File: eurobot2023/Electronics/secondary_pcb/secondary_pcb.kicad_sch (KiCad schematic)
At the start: 34 parts, among them IC1 CD74HCT125M96, IC2 SN74LVC126ADR, J1 PI40HAT, J10 Conn_01x02_Male, J11 MagneticEncoder, J12 Conn_01x07_Male, J13 MagneticEncoder, J14 Conn_01x03_Male, J15 Conn_01x02_Male, J2 Conn_01x02_Male, J3 Conn_01x02_Male, J4 Conn_01x02_Male, J5 Conn_01x02_Male, J6 Conn_01x02_Male, J7 Conn_01x02_Male, J9 22-03-5035, P1 R-78Bxx-2.0, P2 Amazon 5A stepdown, U1 MCP2515-xSO, U2 TJA1049T, U3 PCA9306D, U4 Pololu_MAX14870, U5 PCA9685PW

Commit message: Modify secondary pcb
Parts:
- removed C3: Conn_03x08, MiAM:Pin_Header_Straight_3x08_Pitch2.54mm, symbol MiAM:Conn_03x08
- removed J14: Conn_01x03_Male, Connector_PinHeader_2.54mm:PinHeader_1x03_P2.54mm_Vertical, symbol Connector:Conn_01x03_Male
- removed U3: PCA9306D, Package_SO:SO-8_3.9x4.9mm_P1.27mm, symbol Interface:PCA9306D
- removed U5: PCA9685PW, Package_SO:TSSOP-28_4.4x9.7mm_P0.65mm, symbol Driver_LED:PCA9685PW
- added I2C2, I2C3: Conn_01x05_Male, Connector_PinHeader_2.54mm:PinHeader_1x05_P2.54mm_Vertical, symbol Connector:Conn_01x05_Male
- added Mot V Select: Conn_01x03_Male, Connector_PinHeader_2.54mm:PinHeader_1x03_P2.54mm_Vertical, symbol Connector:Conn_01x03_Male
- Enc 1: renamed from J11
- Enc 2: renamed from J13
- IC1, IC2: footprint SOIC127P600X175-14N -> MiAM:SOIC127P600X175-14N
- Servo: renamed from J9; footprint SHDR3W60P0X250_1X3_990X490X590P -> MiAM:SHDR3W60P0X250_1X3_990X490X590P
- renumbered J7 to CAN1, J15 to CAN2, C4 to GPIO, J12 to I2C1, J10 to Mot
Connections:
- net +24V: now also Mot V Select.3 (Pin_3)
- net +3.3V: now also I2C2.1 (Pin_1), I2C3.1 (Pin_1)
- net +7.5V: now also Mot V Select.1 (Pin_1); no longer U4.9 (Vin)
- net GND: now also I2C2.2 (Pin_2), I2C3.2 (Pin_2)
- net I2C SCL: now also I2C2.3 (Pin_3), I2C3.3 (Pin_3)
- net I2C SDA: now also I2C2.4 (Pin_4), I2C3.4 (Pin_4)
- net GPIO 13: now reaches J1.33 (BCM13)
- net GPIO 13: now also I2C2.5 (Pin_5)
- net GPIO 19: now reaches J1.35 (BCM19)
- net GPIO 19: now also I2C3.5 (Pin_5)
- new net: Mot V Select.2 (Pin_2), U4.9 (Vin)
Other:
- note added: "DC motor"
- note added: "Encoders"
- note added: "Raspberry Pi"
- note removed: "Pump & other DC motor"
- note removed: "RC servos"
- note removed: "Servo driver"
- note removed: "[TODO] - Transistor for power switch"
- company: (none) -> MiAM Robotics Inc.
- title: (none) -> Secondary Robot PCB
- moved on the sheet: C1, C2, CAN1, CAN2, D2, D3, Enc 1, Enc 2, GPIO, HC49, I2C1, IC1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

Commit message: Begin routing
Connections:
- net UART_RX_5 is gone; now on net UART_HD: IC2.5 (2A)
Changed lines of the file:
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@@
     (effects (font (size 1.27 1.27)) (justify left bottom))
   )
-  (label "UART_RX_5" (at 115.57 95.25 180)
+  (label "UART_HD" (at 115.57 95.25 180)
     (effects (font (size 1.27 1.27)) (justify right bottom))
   )

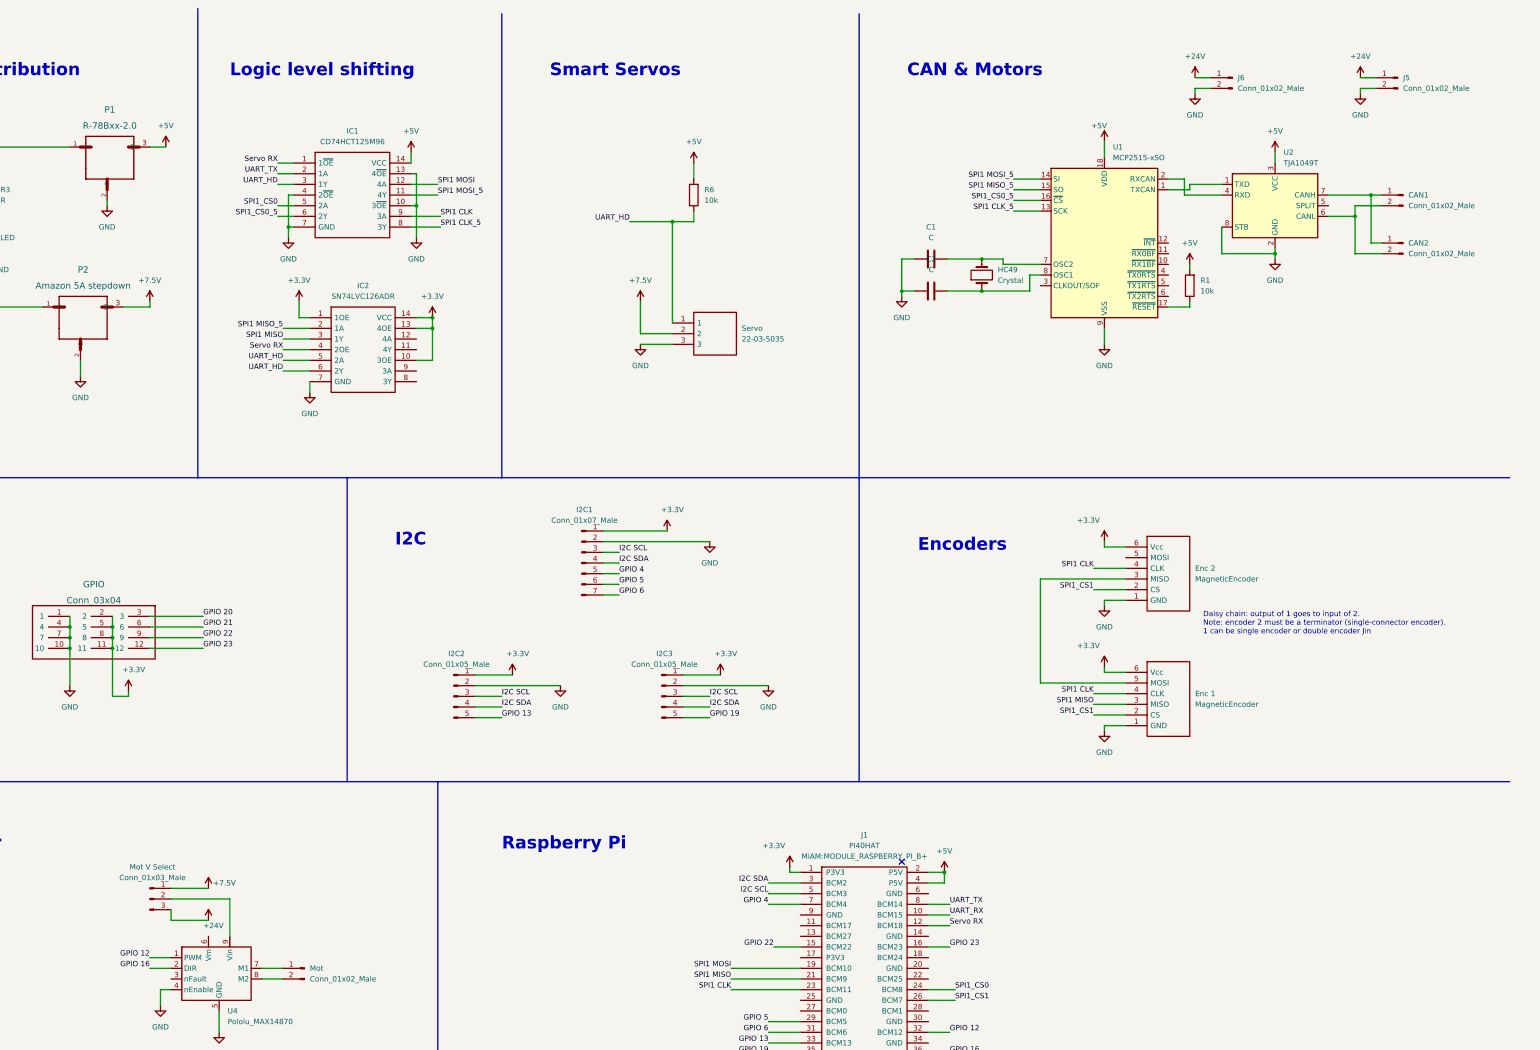
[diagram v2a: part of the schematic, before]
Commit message: Electronics: correct PCB schematic and component references.
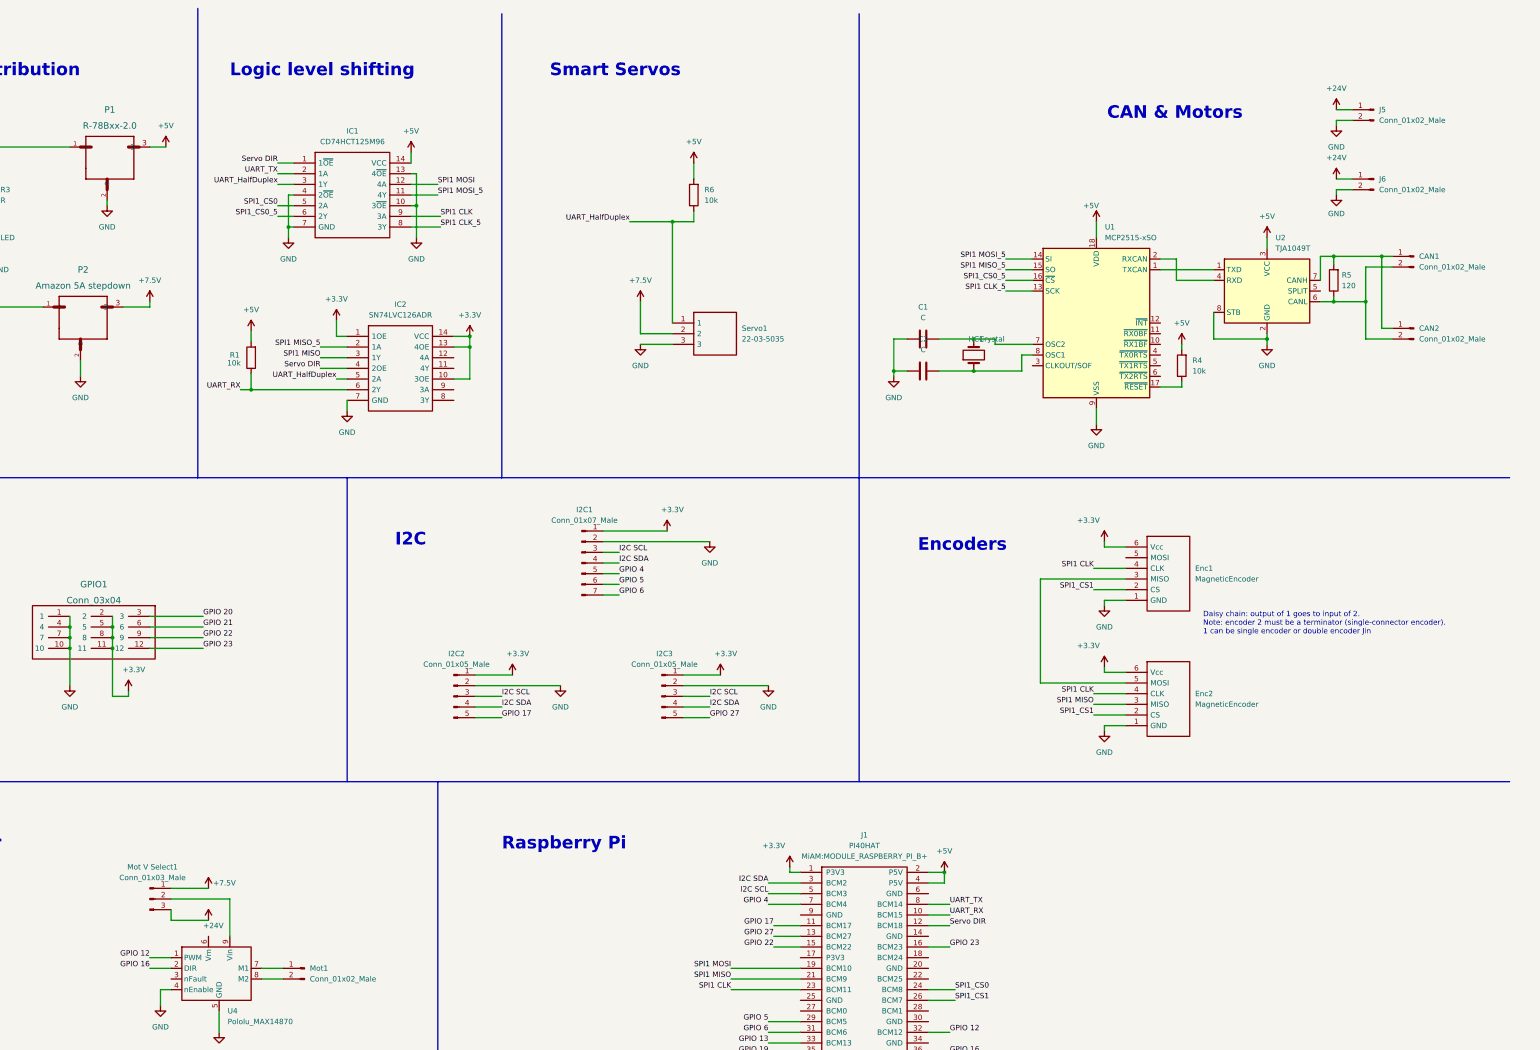
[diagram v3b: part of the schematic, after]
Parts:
- removed HC49: Crystal, Crystal:Crystal_HC49-4H_Vertical, symbol Device:Crystal
- added HC1: Crystal, Crystal:Crystal_HC49-4H_Vertical, symbol Device:Crystal
- added R4: 10k, Resistor_SMD:R_0805_2012Metric, symbol Device:R
- added R5: 120, Resistor_THT:R_Axial_DIN0309_L9.0mm_D3.2mm_P12.70mm_Horizontal, symbol Device:R
- C1, C2: footprint Capacitor_THT:C_Rect_L10.0mm_W2.5mm_P7.50mm_MKS4 -> Capacitor_THT:C_Disc_D8.0mm_W5.0mm_P10.00mm
- Enc1: renamed from Enc 2
- Enc2: renamed from Enc 1
- IC2: footprint MiAM:SOIC127P600X175-14N -> SOIC127P600X175-14N
- Mot V Select1: renamed from Mot V Select
- P1: RS Recom R-78B5.0-2.0 -> 139-2959
- R1: footprint Resistor_THT:R_Axial_DIN0309_L9.0mm_D3.2mm_P12.70mm_Horizontal -> Resistor_SMD:R_0805_2012Metric
- renumbered GPIO to GPIO1, Mot to Mot1, Servo to Servo1
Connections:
- net +5V: now also R4.2
- net GPIO 13: no longer I2C2.5 (Pin_5)
- net GPIO 19: no longer I2C3.5 (Pin_5)
- net UART_RX: now also IC2.6 (2Y), R1.1
- net at CAN1.2 (Pin_2), CAN2.2 (Pin_2), U2.6 (CANL): now also R5.1
- net at CAN1.1 (Pin_1), CAN2.1 (Pin_1), U2.7 (CANH): now also R5.2
- net at C2.2, U1.8 (OSC1): now also HC1.1
- net at C1.2, U1.7 (OSC2): now also HC1.2
- net at U1.17 (~{RESET}): now also R4.1; no longer R1.1
- net GPIO 17: now reaches J1.11 (BCM17)
- net GPIO 17: now also I2C2.5 (Pin_5)
- net GPIO 27: now reaches J1.13 (BCM27)
- net GPIO 27: now also I2C3.5 (Pin_5)
- net Servo RX renamed Servo DIR
- net UART_HD renamed UART_HalfDuplex
- net UART_HalfDuplex: no longer IC2.6 (2Y)
- no-connect marks 1 -> 0

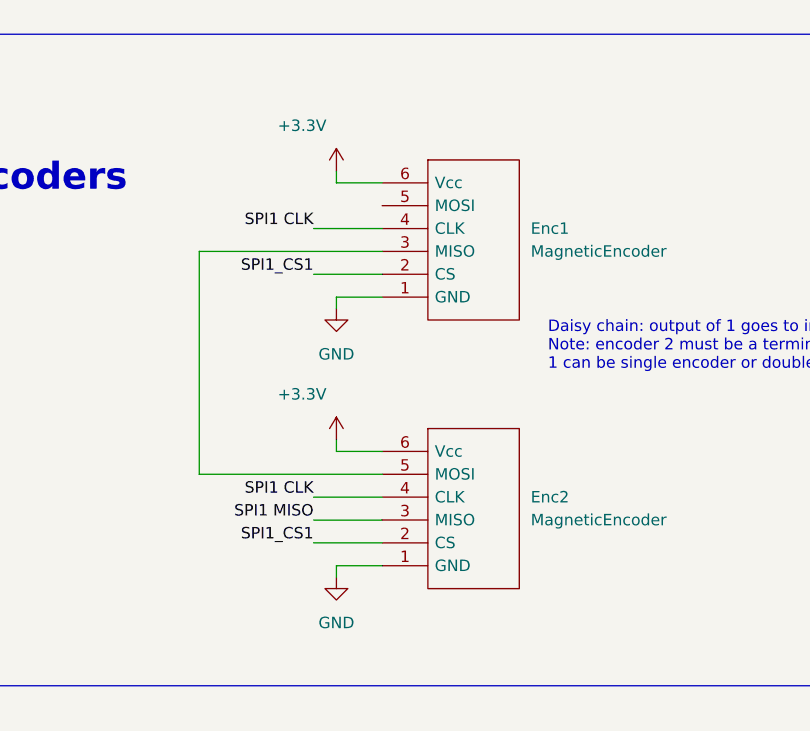
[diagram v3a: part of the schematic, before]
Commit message: Electronics: update PCB
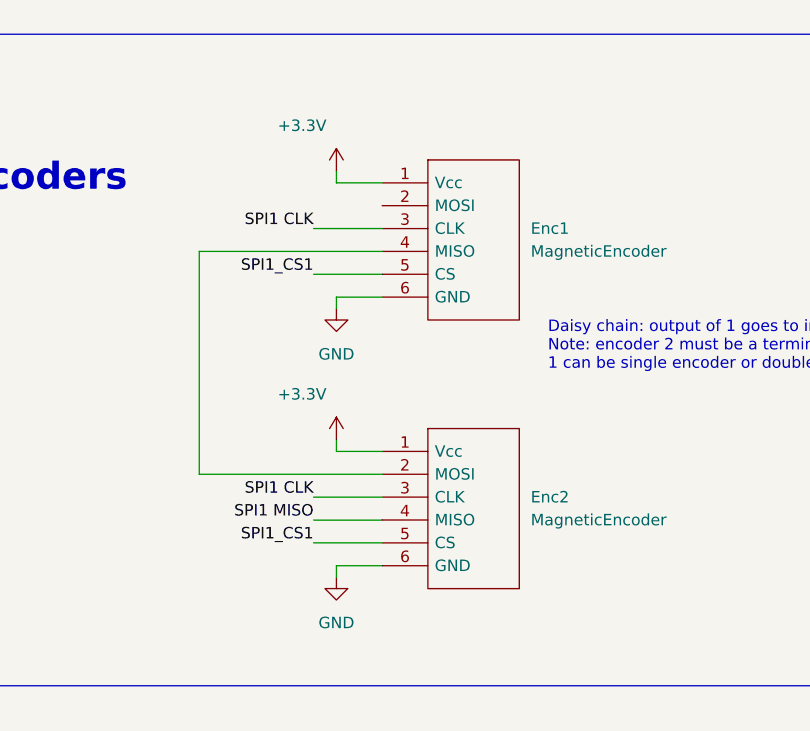
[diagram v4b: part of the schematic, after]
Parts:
- R2, R3, R5: footprint Resistor_THT:R_Axial_DIN0309_L9.0mm_D3.2mm_P12.70mm_Horizontal -> Resistor_SMD:R_0805_2012Metric
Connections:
- net +3.3V: now also Enc1.1 (Vcc), Enc2.1 (Vcc); no longer Enc1.6 (Vcc), Enc2.6 (Vcc)
- net GND: now also Enc1.6 (GND), Enc2.6 (GND); no longer Enc1.1 (GND), Enc2.1 (GND)
- net SPI1 CLK: now also Enc1.3 (CLK), Enc2.3 (CLK); no longer Enc1.4 (CLK), Enc2.4 (CLK)
- net SPI1 MISO: now also Enc2.4 (MISO); no longer Enc2.3 (MISO)
- net SPI1_CS1: now also Enc1.5 (CS), Enc2.5 (CS); no longer Enc1.2 (CS), Enc2.2 (CS)
- new net: Enc1.4 (MISO), Enc2.2 (MOSI)
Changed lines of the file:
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@@
       (effects (font (size 1.27 1.27)) (justify right))
     )
-    (property "Footprint" "Resistor_THT:R_Axial_DIN0309_L9.0mm_D3.2mm_P12.70mm_Horizontal" (id 2) (at 367.538 76.2 90)
+    (property "Footprint" "Resistor_SMD:R_0805_2012Metric" (id 2) (at 367.538 76.2 90)
       (effects (font (size 1.27 1.27)) hide)
     )
@@
       (effects (font (size 1.27 1.27)) (justify right))
     )
-    (property "Footprint" "Resistor_THT:R_Axial_DIN0309_L9.0mm_D3.2mm_P12.70mm_Horizontal" (id 2) (at 47.498 55.88 90)
+    (property "Footprint" "Resistor_SMD:R_0805_2012Metric" (id 2) (at 47.498 55.88 90)
       (effects (font (size 1.27 1.27)) hide)
     )
@@
       (effects (font (size 1.27 1.27)) (justify right))
     )
-    (property "Footprint" "Resistor_THT:R_Axial_DIN0309_L9.0mm_D3.2mm_P12.70mm_Horizontal" (id 2) (at 36.068 91.44 90)
+    (property "Footprint" "Resistor_SMD:R_0805_2012Metric" (id 2) (at 36.068 91.44 90)
       (effects (font (size 1.27 1.27)) hide)
     )
@@
     (pin "3")
   )
-  (symbol (lib_id "MiAM:MagneticEncoder") (at 316.23 139.7 0) (unit 1)
+  (symbol (lib_name "MagneticEncoder_1") (lib_id "MiAM:MagneticEncoder") (at 316.23 139.7 0) (unit 1)
     (in_bom yes) (on_board yes) (fields_autoplaced)
     (property "Reference" "Enc1" (id 0) (at 332.74 144.7799 0)
@@
     )
     (path "/8cd8af2a-beda-42be-a4f0-fe56aaaef64a"
-      (reference "R2") (unit 1) (value "R") (footprint "Resistor_THT:R_Axial_DIN0309_L9.0mm_D3.2mm_P12.70mm_Horizontal")
+      (reference "R2") (unit 1) (value "R") (footprint "Resistor_SMD:R_0805_2012Metric")
     )
     (path "/8b0eec51-c081-4a20-b848-d05ba5caa814"
-      (reference "R3") (unit 1) (value "R") (footprint "Resistor_THT:R_Axial_DIN0309_L9.0mm_D3.2mm_P12.70mm_Horizontal")
+      (reference "R3") (unit 1) (value "R") (footprint "Resistor_SMD:R_0805_2012Metric")
     )
     (path "/c158db55-fd5a-46d4-84d2-bf315f1b7487"
@@
     )
     (path "/3ccac1d3-ad9f-47fc-a87f-7a80712c8d62"
-      (reference "R5") (unit 1) (value "120") (footprint "Resistor_THT:R_Axial_DIN0309_L9.0mm_D3.2mm_P12.70mm_Horizontal")
+      (reference "R5") (unit 1) (value "120") (footprint "Resistor_SMD:R_0805_2012Metric")
     )
     (path "/0b2324c2-ebae-4281-8010-7504e7b6873a"

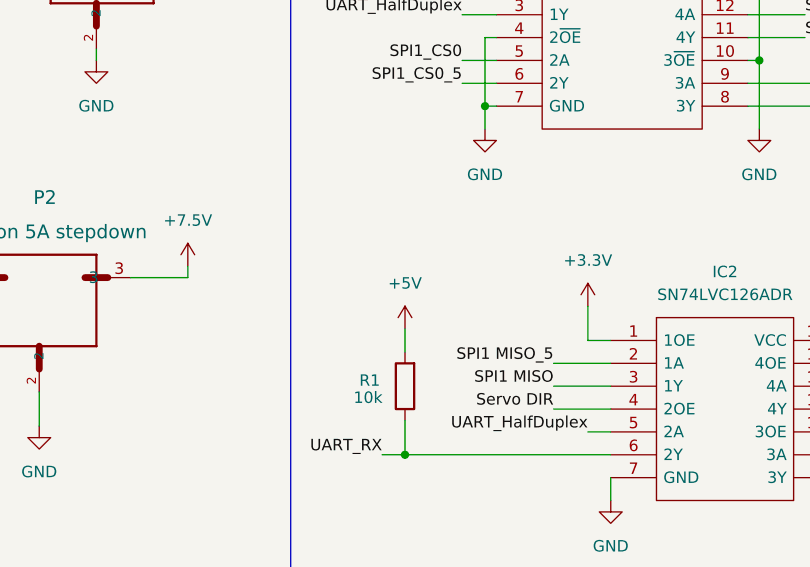
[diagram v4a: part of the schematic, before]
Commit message: Secondary PCB: full version with DRC ok.
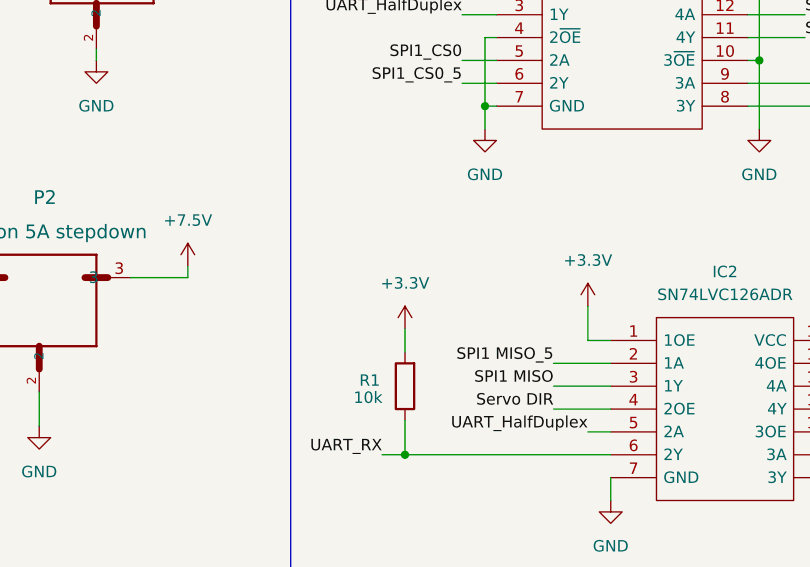
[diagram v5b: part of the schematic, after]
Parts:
- R6: footprint Resistor_THT:R_Axial_DIN0309_L9.0mm_D3.2mm_P12.70mm_Horizontal -> Resistor_SMD:R_0805_2012Metric
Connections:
- net +3.3V: now also R1.2
- net +5V: no longer R1.2
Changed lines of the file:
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@@
       (effects (font (size 1.27 1.27)) (justify right))
     )
-    (property "Footprint" "Resistor_THT:R_Axial_DIN0309_L9.0mm_D3.2mm_P12.70mm_Horizontal" (id 2) (at 215.138 55.88 90)
+    (property "Footprint" "Resistor_SMD:R_0805_2012Metric" (id 2) (at 215.138 55.88 90)
       (effects (font (size 1.27 1.27)) hide)
     )
@@
     (pin "9")
   )
-  (symbol (lib_id "power:+5V") (at 107.95 88.265 0) (unit 1)
-    (in_bom yes) (on_board yes) (fields_autoplaced)
-    (property "Reference" "#PWR0105" (id 0) (at 107.95 92.075 0)
-      (effects (font (size 1.27 1.27)) hide)
-    )
-    (property "Value" "+5V" (id 1) (at 107.95 83.185 0))
-    (property "Footprint" "" (id 2) (at 107.95 88.265 0)
-      (effects (font (size 1.27 1.27)) hide)
-    )
-    (property "Datasheet" "" (id 3) (at 107.95 88.265 0)
-      (effects (font (size 1.27 1.27)) hide)
-    )
-    (pin "1")
-  )
   (symbol (lib_id "power:GND") (at 64.77 172.72 0) (unit 1)
     (in_bom yes) (on_board yes) (fields_autoplaced)
@@
     (pin "8")
     (pin "9")
+  )
+  (symbol (lib_id "power:+3.3V") (at 107.95 88.265 0) (unit 1)
+    (in_bom yes) (on_board yes) (fields_autoplaced)
+    (property "Reference" "#PWR?" (id 0) (at 107.95 92.075 0)
+      (effects (font (size 1.27 1.27)) hide)
+    )
+    (property "Value" "+3.3V" (id 1) (at 107.95 83.185 0))
+    (property "Footprint" "" (id 2) (at 107.95 88.265 0)
+      (effects (font (size 1.27 1.27)) hide)
+    )
+    (property "Datasheet" "" (id 3) (at 107.95 88.265 0)
+      (effects (font (size 1.27 1.27)) hide)
+    )
+    (pin "1")
   )
   (symbol (lib_id "power:GND") (at 45.72 74.93 0) (unit 1)
@@
       (reference "#PWR0104") (unit 1) (value "+3.3V") (footprint "")
     )
-    (path "/3a69cbac-169e-48b5-b5ce-6298d03e7001"
-      (reference "#PWR0105") (unit 1) (value "+5V") (footprint "")
-    )
     (path "/72894b86-2212-4a36-9be0-8e5b526f1a1e"
       (reference "#PWR0106") (unit 1) (value "GND") (footprint "")
@@
       (reference "#PWR0148") (unit 1) (value "+3.3V") (footprint "")
     )
+    (path "/49032196-12fe-4141-bb29-ee6cdbb5d8ee"
+      (reference "#PWR?") (unit 1) (value "+3.3V") (footprint "")
+    )
     (path "/7d5f7387-88d2-4a9e-aece-db6d70feb6c5"
       (reference "C1") (unit 1) (value "C") (footprint "Capacitor_THT:C_Disc_D8.0mm_W5.0mm_P10.00mm")
@@
     )
     (path "/0b2324c2-ebae-4281-8010-7504e7b6873a"
-      (reference "R6") (unit 1) (value "10k") (footprint "Resistor_THT:R_Axial_DIN0309_L9.0mm_D3.2mm_P12.70mm_Horizontal")
+      (reference "R6") (unit 1) (value "10k") (footprint "Resistor_SMD:R_0805_2012Metric")
     )
     (path "/c4c736d4-965b-4f3c-8867-f2b0ac9fcbb3"

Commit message: Minor PCB fixups.
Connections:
- net GPIO 13: no longer names the net of J1.33 (BCM13)
- net GPIO 19: no longer names the net of J1.35 (BCM19)
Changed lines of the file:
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@@
   (junction (at 260.985 97.79) (diameter 0) (color 0 0 0 0)
   )
-  (wire (pts (xy 231.14 257.81) (xy 238.76 257.81))
-    (stroke (width 0) (type default) (color 0 0 0 0))
-  )
   (wire (pts (xy 124.46 92.075) (xy 130.81 92.075))
     (stroke (width 0) (type default) (color 0 0 0 0))
@@
   )
   (wire (pts (xy 40.64 81.28) (xy 40.64 82.55))
-    (stroke (width 0) (type default) (color 0 0 0 0))
-  )
-  (wire (pts (xy 231.14 260.35) (xy 238.76 260.35))
     (stroke (width 0) (type default) (color 0 0 0 0))
   )
@@
     (effects (font (size 1.27 1.27)) (justify left bottom))
   )
-  (label "GPIO 19" (at 231.14 260.35 180)
-    (effects (font (size 1.27 1.27)) (justify right bottom))
-  )
   (label "I2C SDA" (at 167.64 177.8 0)
     (effects (font (size 1.27 1.27)) (justify left bottom))
@@
     (effects (font (size 1.27 1.27)) (justify right bottom))
   )
-  (label "GPIO 13" (at 231.14 257.81 180)
-    (effects (font (size 1.27 1.27)) (justify right bottom))
-  )
